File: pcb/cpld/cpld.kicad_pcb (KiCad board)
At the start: 2 copper layers, 104.4 x 82.7 mm, 32 parts, among them J1 Micro_SD_Card_Det1, J2 Bus_ISA_8bit_AB_Rev0, J3 Atmel-JTAG-10, SW1 ADDR SEL, U1 ATF1504AS-xJx44, U2 AMS1117-3.3, U3 74LVC125, U4 74HCT688, X1 16MHz

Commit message: Prepare Slot-otter v1.1.0 with CPLD revision 1.0 hardware (#7)
* Incrementing version number

* Restore DOS CRLF line endings in updated source files (#5)

* Expanding explanation and polishing settings interface

* Increasing maximum number of files per folder

* Fixing files for MSDOS

* Initial commit SD-CARD write routines

* Improving commenting and routines

* Tuning write cycles

* Improving schematic, improving sd commands and making cross-compilation more convenient

* Adding JLCPCB numbers

* Implementing folder creation

* Refactoring otternav and initial commit copying from HD to SD

* Refining CPLD card

* Initial commit DRIVER

* Working RW driver

* Consolidation step

* Consolidating for v1.0.0 of the driver

* Adding CPLD logic

* Redesigning CPLD PCB

* Final tweaks CPLD

* Refactoring for release

* Improving README.md

* Keep CPLD fabrication archive in sync with Gerber exports

* Prepare Slot-otter 1.1.0 hardware and software release

* Display README hardware renders side by side

* Show Nightwatch screenshot in the user guide
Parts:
- removed G***: LOGO, components:slototter-logo
- removed J3: Atmel-JTAG-10, Connector_IDC:IDC-Header_2x05_P2.54mm_Vertical
- removed TP1: ~{CS}, TestPoint:TestPoint_Loop_D2.54mm_Drill1.5mm_Beaded
- removed TP2: CLK, TestPoint:TestPoint_Loop_D2.54mm_Drill1.5mm_Beaded
- removed TP3: MOSI, TestPoint:TestPoint_Loop_D2.54mm_Drill1.5mm_Beaded
- removed TP4: MISO, TestPoint:TestPoint_Loop_D2.54mm_Drill1.5mm_Beaded
- removed TP5, TP6: GND, TestPoint:TestPoint_Loop_D2.54mm_Drill1.5mm_Beaded
- added SYM1: ~, components:slototter-logo-v2, F.Cu at (137.4, 65.0)
- added SYM2: ~, Symbol:OSHW-Logo_11.4x12mm_SilkScreen, F.Cu at (108.2, 86.9)
- U1: value ATF1504AS-xJx44 -> ATF1504AS
- moved X1 43.1 mm to (121.5, 86.0)
- moved SW1 32.7 mm to (118.4, 104.3)
- moved C7 32.6 mm to (116.4, 83.1)
- moved C3 29.0 mm to (161.2, 72.6)
- moved U1 29.0 mm to (159.6, 80.2)
- moved C2 29.0 mm to (172.3, 86.3)
- moved C4 29.0 mm to (144.4, 86.3)
- moved C5 29.0 mm to (158.0, 100.6)
- moved U4 23.2 mm to (97.4, 100.8), turned to 0 degrees
- moved RN2 22.2 mm to (107.5, 101.0), turned to 180 degrees
- moved R1 20.3 mm to (153.0, 100.6)
- moved C1 17.7 mm to (97.4, 90.6), turned to 0 degrees
- moved RN1 17.5 mm to (87.2, 101.2), turned to 0 degrees
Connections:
- R1 pad 2: Net-(R1-Pad2) -> /MISO_PULL
- U1 pad 12: unconnected-(U1-I/O-Pad12) -> MISO
- U1 pad 13: TMS -> unconnected-(U1-I/O/TMS-Pad13)
- U1 pad 16: ~{RD} -> unconnected-(U1-I/O-Pad16)
- U1 pad 17: ~{WR} -> A0
- U1 pad 18: A0 -> ~{RD}
- U1 pad 2: unconnected-(U1-I/OE2/GCLK2-Pad2) -> 16MHz
- U1 pad 20: unconnected-(U1-I/O-Pad20) -> ~{WR}
- U1 pad 21: unconnected-(U1-I/O-Pad21) -> DB0
- U1 pad 24: MOSI -> /MISO_PULL
- U1 pad 25: MISO -> DB1
- U1 pad 26: Net-(R1-Pad2) -> DB2
- U1 pad 27: ~{CS} -> DB3
- U1 pad 28: CLK -> DB4
- U1 pad 29: DB0 -> DB5
- U1 pad 31: DB1 -> DB6
- U1 pad 32: TCK -> unconnected-(U1-I/O/TCK-Pad32)
- U1 pad 33: DB2 -> DB7
- U1 pad 34: DB3 -> unconnected-(U1-I/O-Pad34)
- U1 pad 36: DB4 -> unconnected-(U1-I/O-Pad36)
- U1 pad 37: DB5 -> unconnected-(U1-I/O-Pad37)
- U1 pad 38: TDO -> unconnected-(U1-I/O/TDO-Pad38)
- U1 pad 39: DB6 -> unconnected-(U1-I/O-Pad39)
- U1 pad 4: unconnected-(U1-I/O-Pad4) -> CLK
- U1 pad 40: DB7 -> ~{CS}
- U1 pad 43: 16MHz -> unconnected-(U1-I/GCLK1-Pad43)
- U1 pad 44: ~{PORTSEL} -> unconnected-(U1-I/OE1-Pad44)
- U1 pad 6: unconnected-(U1-I/O-Pad6) -> MOSI
- U1 pad 7: TDI -> unconnected-(U1-I/O/TDI-Pad7)
- U1 pad 9: unconnected-(U1-I/O-Pad9) -> ~{PORTSEL}
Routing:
- net GND: track 690.0 -> 476.1 mm, vias 29 -> 11
- net ~{CS}: track 163.0 -> 32.9 mm, vias 3 -> 1
- net CLK: track 131.6 -> 37.1 mm, vias 1 -> 0
- net MOSI: track 110.3 -> 40.0 mm, vias 5 -> 0
- net MISO: track 127.1 -> 63.6 mm, vias 1 -> 2
- net A8: track 67.6 -> 18.0 mm, vias 0 -> 2
- net A7: track 66.3 -> 17.0 mm, vias 0 -> 2
- net A9: track 69.3 -> 20.2 mm, vias 0 -> 2
- net TDI: track 47.8 -> 0.00 mm, vias 2 -> 0
- net A6: track 63.6 -> 16.2 mm
- net TMS: track 41.8 -> 0.00 mm, vias 2 -> 0
- net VCC: track 444.7 -> 409.5 mm, vias 21 -> 11
- net 16MHz: track 54.8 -> 21.1 mm, vias 2 -> 0
- net A0: track 60.8 -> 90.4 mm
- net A1: track 62.0 -> 90.8 mm
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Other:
- board size 104.4 x 82.7 mm -> 104.4 x 82.5 mm
- board text added: "CPLD rev 1.0"
- board text removed: "SLOT-OTTER"
- board text removed: "jlcjlcjlcjlc"

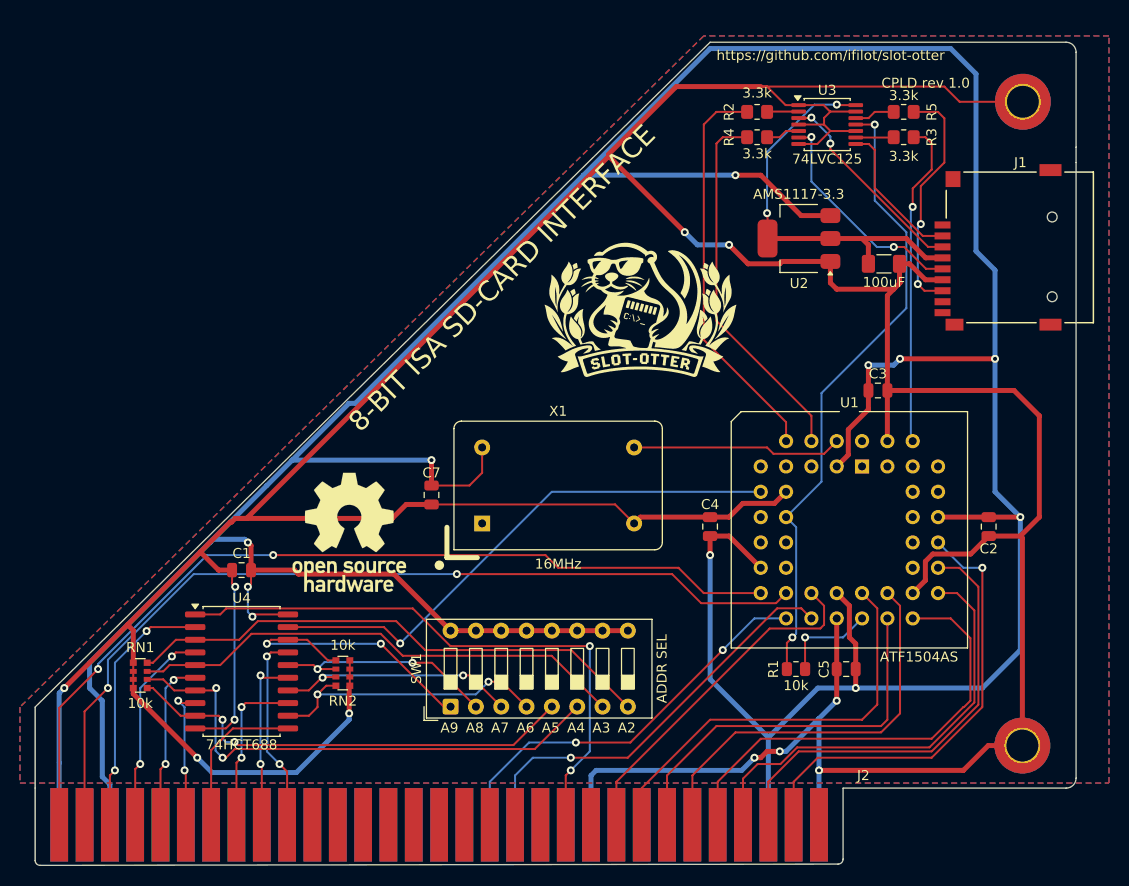
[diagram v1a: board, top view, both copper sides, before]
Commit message: Tuning lay-out of CPLD and improving README>md
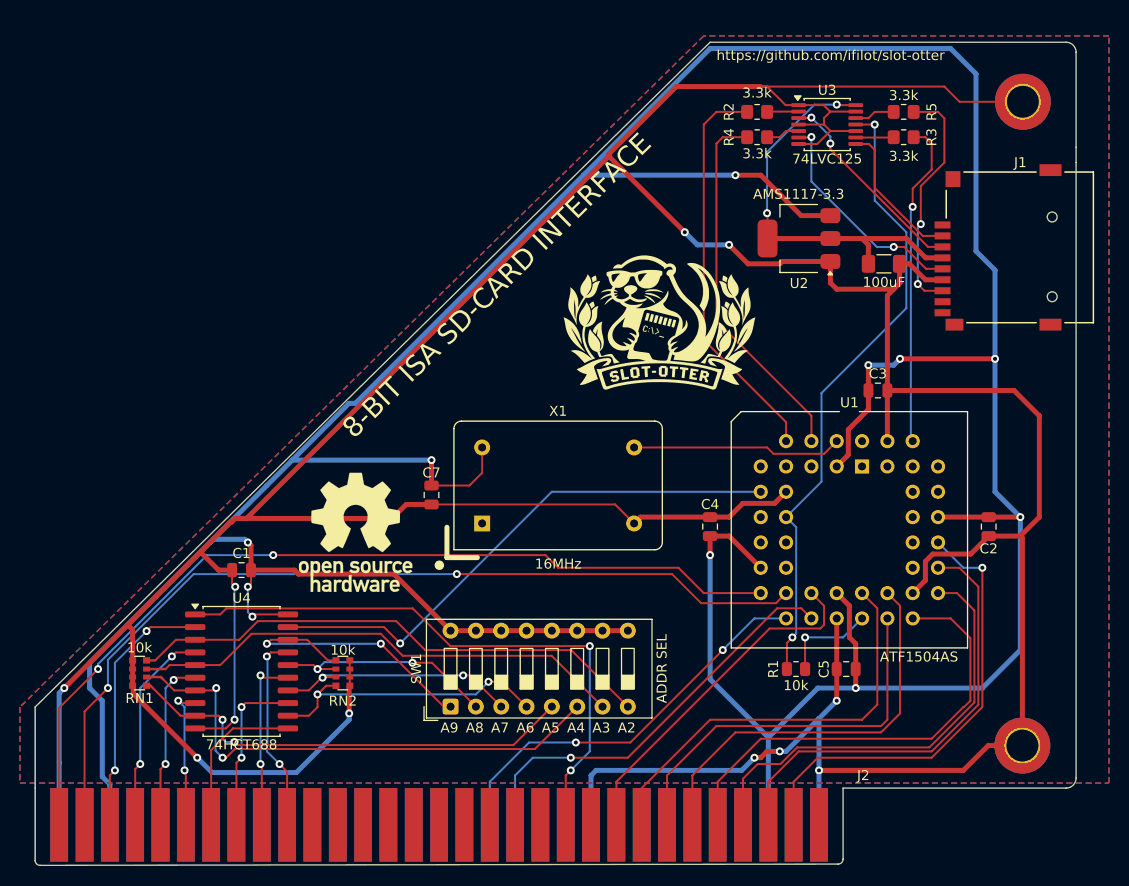
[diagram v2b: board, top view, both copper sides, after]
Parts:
- moved SYM1 2.29 mm to (139.3, 66.3)
- moved SYM2 0.63 mm to (108.8, 86.9)
- moved RN1 0.24 mm to (87.2, 101.0)
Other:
- board text removed: "CPLD rev 1.0"

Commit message: Revising CPLD board and adding OSHWA certification
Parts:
- added SYM3: oshw-certificate, components:oshwa_h15, F.Cu at (145.0, 66.5)
- added SYM4: kicad-logo, Symbol:KiCad-Logo2_5mm_SilkScreen, F.Cu at (108.9, 89.4)
- SYM1: value ~ -> otterlogo; footprint components:slototter-logo-v2 -> components:slototter-logo-v2_h12
- SYM2: value ~ -> oshw-logo; footprint Symbol:OSHW-Logo_11.4x12mm_SilkScreen -> Symbol:OSHW-Logo_7.5x8mm_SilkScreen
- moved SYM1 9.02 mm to (130.3, 66.0)
- moved SYM2 6.13 mm to (109.5, 80.8)
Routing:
- net GND: vias 11 -> 122
- added copper zone on B.Cu, net GND
- removed copper zone on B.Cu, net VCC
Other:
- board text added: "8-BIT ISA SD-CARD adapter"
- board text removed: "8-BIT ISA SD-CARD INTERFACE"
